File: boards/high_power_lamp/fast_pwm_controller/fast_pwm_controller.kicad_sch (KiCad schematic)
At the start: 22 parts, among them J1 Screw_Terminal_01x02, J2 Screw_Terminal_01x02, J3 Screw_Terminal_01x02, J4 Screw_Terminal_01x02, J5 Screw_Terminal_01x02, J6 Screw_Terminal_01x02, J7 Screw_Terminal_01x02, J8 Screw_Terminal_01x02, J9 Screw_Terminal_01x02, U2 TLC3704

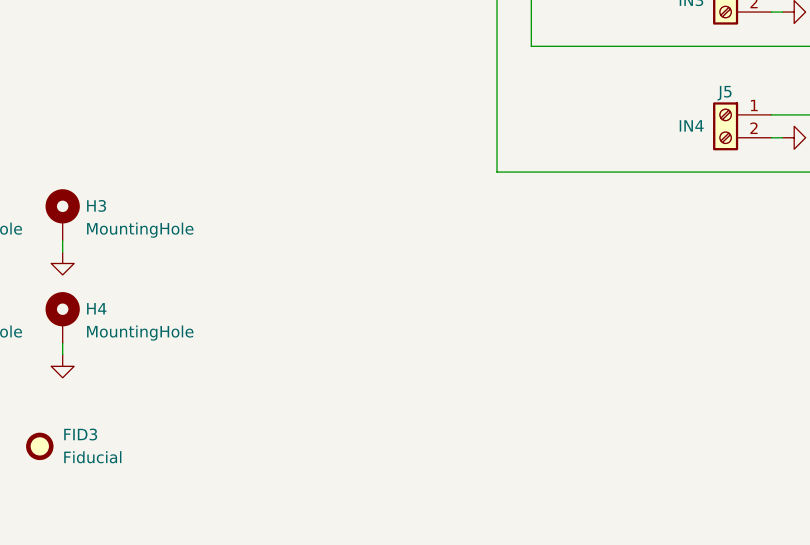
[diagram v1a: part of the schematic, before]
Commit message: basic external layout of board
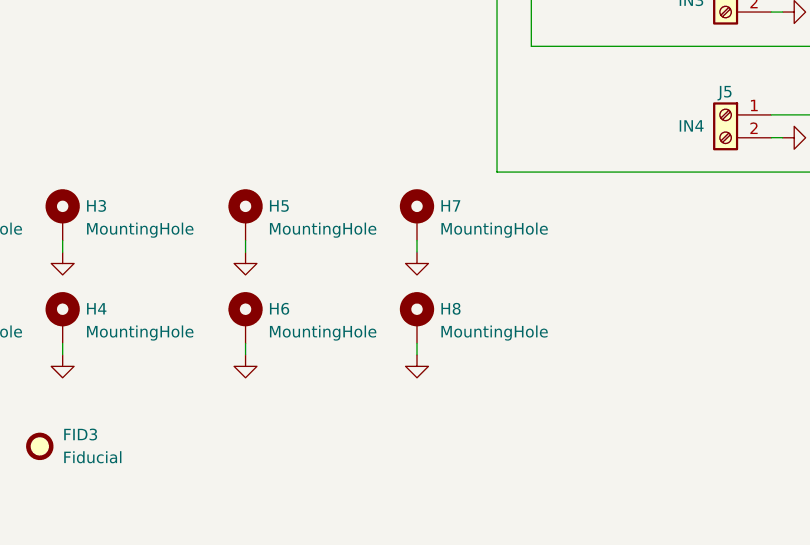
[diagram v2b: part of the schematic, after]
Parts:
- added H5, H6, H7, H8: MountingHole, MountingHole:MountingHole_3.2mm_M3_DIN965_Pad, symbol Mechanical:MountingHole_Pad
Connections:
- net GND: now also H5.1, H6.1, H7.1, H8.1

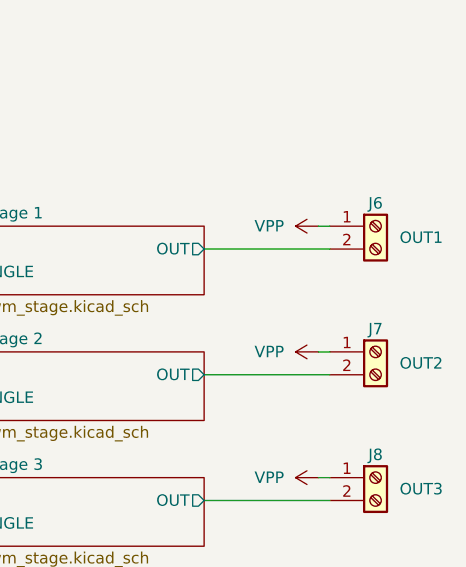
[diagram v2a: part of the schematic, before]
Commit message: almost finish arranging the fast pwm controller pcb
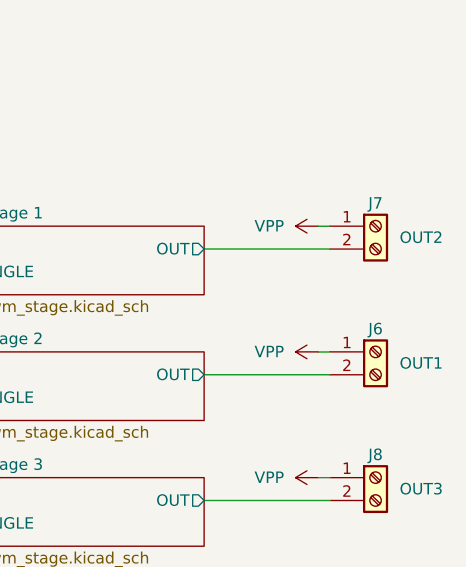
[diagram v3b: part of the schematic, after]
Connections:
- net PWM stage 1/OUT: now also J7.2 (Pin_2); no longer J6.2 (Pin_2)
- net PWM stage 2/OUT: now also J6.2 (Pin_2); no longer J7.2 (Pin_2)
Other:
- moved on the sheet: J6, J7
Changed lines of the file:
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@@
     )
   )
-  (symbol (lib_id "Connector:Screw_Terminal_01x02") (at 208.28 93.98 0) (unit 1)
+  (symbol (lib_id "Connector:Screw_Terminal_01x02") (at 208.28 107.95 0) (unit 1)
     (in_bom yes) (on_board yes) (dnp no)
-    (property "Reference" "J6" (at 208.28 91.44 0)
+    (property "Reference" "J6" (at 208.28 105.41 0)
       (effects (font (size 1.27 1.27)))
     )
-    (property "Value" "Screw_Terminal_01x02" (at 208.28 100.33 0)
+    (property "Value" "Screw_Terminal_01x02" (at 208.28 114.3 0)
       (effects (font (size 1.27 1.27)) hide)
     )
-    (property "Footprint" "TerminalBlock_Philmore:TerminalBlock_Philmore_TB132_1x02_P5.00mm_Horizontal" (at 208.28 93.98 0)
+    (property "Footprint" "TerminalBlock_Philmore:TerminalBlock_Philmore_TB132_1x02_P5.00mm_Horizontal" (at 208.28 107.95 0)
       (effects (font (size 1.27 1.27)) hide)
     )
-    (property "Datasheet" "~" (at 208.28 93.98 0)
+    (property "Datasheet" "~" (at 208.28 107.95 0)
       (effects (font (size 1.27 1.27)) hide)
     )
-    (property "Purpose" "OUT1" (at 213.36 95.25 0)
+    (property "Purpose" "OUT1" (at 213.36 109.22 0)
       (effects (font (size 1.27 1.27)))
     )
@@
     )
   )
-  (symbol (lib_id "Connector:Screw_Terminal_01x02") (at 208.28 107.95 0) (unit 1)
+  (symbol (lib_id "Connector:Screw_Terminal_01x02") (at 208.28 93.98 0) (unit 1)
     (in_bom yes) (on_board yes) (dnp no)
-    (property "Reference" "J7" (at 208.28 105.41 0)
+    (property "Reference" "J7" (at 208.28 91.44 0)
       (effects (font (size 1.27 1.27)))
     )
-    (property "Value" "Screw_Terminal_01x02" (at 208.28 114.3 0)
+    (property "Value" "Screw_Terminal_01x02" (at 208.28 100.33 0)
       (effects (font (size 1.27 1.27)) hide)
     )
-    (property "Footprint" "TerminalBlock_Philmore:TerminalBlock_Philmore_TB132_1x02_P5.00mm_Horizontal" (at 208.28 107.95 0)
+    (property "Footprint" "TerminalBlock_Philmore:TerminalBlock_Philmore_TB132_1x02_P5.00mm_Horizontal" (at 208.28 93.98 0)
       (effects (font (size 1.27 1.27)) hide)
     )
-    (property "Datasheet" "~" (at 208.28 107.95 0)
+    (property "Datasheet" "~" (at 208.28 93.98 0)
       (effects (font (size 1.27 1.27)) hide)
     )
-    (property "Purpose" "OUT2" (at 213.36 109.22 0)
+    (property "Purpose" "OUT2" (at 213.36 95.25 0)
       (effects (font (size 1.27 1.27)))
     )

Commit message: prepare traces
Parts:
- renumbered J7 to J6, J6 to J7
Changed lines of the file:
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@@
   (symbol (lib_id "Connector:Screw_Terminal_01x02") (at 208.28 107.95 0) (unit 1)
     (in_bom yes) (on_board yes) (dnp no)
-    (property "Reference" "J6" (at 208.28 105.41 0)
+    (property "Reference" "J7" (at 208.28 105.41 0)
       (effects (font (size 1.27 1.27)))
     )
@@
       (project "fast_pwm_controller"
         (path "/ebb02bb0-15d4-41b5-b7b0-053d51d38d86"
-          (reference "J6") (unit 1)
+          (reference "J7") (unit 1)
         )
       )
@@
   (symbol (lib_id "Connector:Screw_Terminal_01x02") (at 208.28 93.98 0) (unit 1)
     (in_bom yes) (on_board yes) (dnp no)
-    (property "Reference" "J7" (at 208.28 91.44 0)
+    (property "Reference" "J6" (at 208.28 91.44 0)
       (effects (font (size 1.27 1.27)))
     )
@@
       (project "fast_pwm_controller"
         (path "/ebb02bb0-15d4-41b5-b7b0-053d51d38d86"
-          (reference "J7") (unit 1)
+          (reference "J6") (unit 1)
         )
       )

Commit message: arrange everything
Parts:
- gave numbers to parts that had none: 1
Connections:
- net +12V: now also U1.1 (VCC)
- net GND: now also U1.11, U1.14, U1.8 (VSS); no longer U1.3, U1.3
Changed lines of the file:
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@@
       )
       (project "fast_pwm_controller"
-        (path "/ebb02bb0-15d4-41b5-b7b0-053d51d38d86/14949cb1-4b69-4c50-91f5-b66762a055b9"
-          (reference "C?") (unit 1)
-        )
         (path "/ebb02bb0-15d4-41b5-b7b0-053d51d38d86"
           (reference "C1") (unit 1)
@@
     )
   )
-  (symbol (lib_id "4xxx:4050") (at 143.51 54.61 0) (unit 1)
-    (in_bom yes) (on_board yes) (dnp no)
-    (property "Reference" "U?" (at 147.32 45.72 0)
+  (symbol (lib_id "4xxx:4050") (at 143.51 54.61 0) (unit 7)
+    (in_bom yes) (on_board yes) (dnp no)
+    (property "Reference" "U1" (at 147.32 45.72 0)
       (effects (font (size 1.27 1.27)))
     )
@@
     (instances
       (project "fast_pwm_controller"
-        (path "/ebb02bb0-15d4-41b5-b7b0-053d51d38d86/1dc02105-34f4-4dcd-909a-a43f3cf6326e"
-          (reference "U?") (unit 1)
-        )
         (path "/ebb02bb0-15d4-41b5-b7b0-053d51d38d86"
           (reference "U1") (unit 7)
@@
     )
   )
-  (symbol (lib_id "4xxx:4050") (at 207.01 50.8 0) (unit 1)
-    (in_bom yes) (on_board yes) (dnp no)
-    (property "Reference" "U?" (at 207.01 45.72 0)
+  (symbol (lib_id "4xxx:4050") (at 207.01 50.8 0) (unit 5)
+    (in_bom yes) (on_board yes) (dnp no)
+    (property "Reference" "U1" (at 207.01 45.72 0)
       (effects (font (size 1.27 1.27)))
     )
@@
     (instances
       (project "fast_pwm_controller"
-        (path "/ebb02bb0-15d4-41b5-b7b0-053d51d38d86/1dc02105-34f4-4dcd-909a-a43f3cf6326e"
-          (reference "U?") (unit 1)
-        )
         (path "/ebb02bb0-15d4-41b5-b7b0-053d51d38d86"
           (reference "U1") (unit 5)
@@
       )
       (project "fast_pwm_controller"
-        (path "/ebb02bb0-15d4-41b5-b7b0-053d51d38d86/14949cb1-4b69-4c50-91f5-b66762a055b9"
-          (reference "C?") (unit 1)
-        )
         (path "/ebb02bb0-15d4-41b5-b7b0-053d51d38d86"
           (reference "C2") (unit 1)
@@
     )
   )
-  (symbol (lib_id "4xxx:4050") (at 207.01 62.23 0) (unit 1)
-    (in_bom yes) (on_board yes) (dnp no)
-    (property "Reference" "U?" (at 207.01 57.15 0)
+  (symbol (lib_id "4xxx:4050") (at 207.01 62.23 0) (unit 6)
+    (in_bom yes) (on_board yes) (dnp no)
+    (property "Reference" "U1" (at 207.01 57.15 0)
       (effects (font (size 1.27 1.27)))
     )
@@
     (instances
       (project "fast_pwm_controller"
-        (path "/ebb02bb0-15d4-41b5-b7b0-053d51d38d86/1dc02105-34f4-4dcd-909a-a43f3cf6326e"
-          (reference "U?") (unit 1)
-        )
         (path "/ebb02bb0-15d4-41b5-b7b0-053d51d38d86"
           (reference "U1") (unit 6)
@@
           (reference "U2") (unit 5)
         )
-        (path "/ebb02bb0-15d4-41b5-b7b0-053d51d38d86/1dc02105-34f4-4dcd-909a-a43f3cf6326e"
-          (reference "U?") (unit 1)
-        )
       )
     )
@@
       (effects (font (size 1.27 1.27)) hide)
     )
-    (property "Value" "+12V" (at 41.91 95.25 0)
+    (property "Value" "+12V" (at 39.37 95.25 90)
       (effects (font (size 1.27 1.27)))
     )
@@
       (effects (font (size 1.27 1.27)) (justify left top))
     )
-    (pin "TRIANGLE_INV" output (at 90.17 97.79 0)
+    (pin "TRIANGLE_INV" output (at 90.17 95.25 0)
       (effects (font (size 1.27 1.27)) (justify right))
     )
-    (pin "TRIANGLE" output (at 90.17 95.25 0)
+    (pin "TRIANGLE" output (at 90.17 97.79 0)
       (effects (font (size 1.27 1.27)) (justify right))
     )

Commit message: finalise board
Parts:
- added TP1, TP2: TestPoint, TestPoint:TestPoint_THTPad_D2.0mm_Drill1.0mm, symbol Connector:TestPoint
- J6: renamed from J9; Purpose OUT4 -> OUT1
- J7: renamed from J8; Purpose OUT3 -> OUT2
- J8: renamed from J6; Purpose OUT2 -> OUT3
- J9: renamed from J7; Purpose OUT1 -> OUT4
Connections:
- net PWM stage 1/OUT: now also J6.2 (Pin_2); no longer J8.2 (Pin_2)
- net PWM stage 1/TRIANGLE: now also TP1.1
- net PWM stage 2/OUT: now also J7.2 (Pin_2); no longer J9.2 (Pin_2)
- net PWM stage 2/TRIANGLE: now also TP2.1
- net PWM stage 3/OUT: now also J8.2 (Pin_2); no longer J7.2 (Pin_2)
- net PWM stage 4/OUT: now also J9.2 (Pin_2); no longer J6.2 (Pin_2)
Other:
- moved on the sheet: J6, J7, J8, J9
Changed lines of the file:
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@@
 (kicad_sch (version 20230121) (generator eeschema)
   (paper "A4")
+  (junction (at 99.06 97.79) (diameter 0) (color 0 0 0 0)
+  )
   (junction (at 115.57 113.03) (diameter 0) (color 0 0 0 0)
   )
@@
   )
   (junction (at 119.38 99.06) (diameter 0) (color 0 0 0 0)
+  )
+  (junction (at 99.06 95.25) (diameter 0) (color 0 0 0 0)
   )
   (junction (at 143.51 38.1) (diameter 0) (color 0 0 0 0)
@@
     (stroke (width 0) (type default))
   )
-  (wire (pts (xy 90.17 97.79) (xy 115.57 97.79))
+  (wire (pts (xy 90.17 97.79) (xy 99.06 97.79))
     (stroke (width 0) (type default))
   )
@@
     (stroke (width 0) (type default))
   )
+  (wire (pts (xy 99.06 95.25) (xy 119.38 95.25))
+    (stroke (width 0) (type default))
+  )
   (wire (pts (xy 146.05 123.19) (xy 147.32 123.19))
     (stroke (width 0) (type default))
@@
     (stroke (width 0) (type default))
   )
-  (wire (pts (xy 90.17 95.25) (xy 119.38 95.25))
+  (wire (pts (xy 90.17 95.25) (xy 99.06 95.25))
     (stroke (width 0) (type default))
   )
@@
   )
   (wire (pts (xy 157.48 58.42) (xy 157.48 69.85))
+    (stroke (width 0) (type default))
+  )
+  (wire (pts (xy 99.06 97.79) (xy 115.57 97.79))
     (stroke (width 0) (type default))
   )
@@
     )
   )
-  (symbol (lib_id "Connector:Screw_Terminal_01x02") (at 208.28 121.92 0) (unit 1)
-    (in_bom yes) (on_board yes) (dnp no)
-    (property "Reference" "J8" (at 208.28 119.38 0)
-      (effects (font (size 1.27 1.27)))
-    )
-    (property "Value" "Screw_Terminal_01x02" (at 208.28 128.27 0)
-      (effects (font (size 1.27 1.27)) hide)
-    )
-    (property "Footprint" "TerminalBlock_Philmore:TerminalBlock_Philmore_TB132_1x02_P5.00mm_Horizontal" (at 208.28 121.92 0)
-      (effects (font (size 1.27 1.27)) hide)
-    )
-    (property "Datasheet" "~" (at 208.28 121.92 0)
-      (effects (font (size 1.27 1.27)) hide)
-    )
-    (property "Purpose" "OUT3" (at 213.36 123.19 0)
+  (symbol (lib_id "Connector:Screw_Terminal_01x02") (at 208.28 107.95 0) (unit 1)
+    (in_bom yes) (on_board yes) (dnp no)
+    (property "Reference" "J7" (at 208.28 105.41 0)
+      (effects (font (size 1.27 1.27)))
+    )
+    (property "Value" "Screw_Terminal_01x02" (at 208.28 114.3 0)
+      (effects (font (size 1.27 1.27)) hide)
+    )
+    (property "Footprint" "TerminalBlock_Philmore:TerminalBlock_Philmore_TB132_1x02_P5.00mm_Horizontal" (at 208.28 107.95 0)
+      (effects (font (size 1.27 1.27)) hide)
+    )
+    (property "Datasheet" "~" (at 208.28 107.95 0)
+      (effects (font (size 1.27 1.27)) hide)
+    )
+    (property "Purpose" "OUT2" (at 213.36 109.22 0)
       (effects (font (size 1.27 1.27)))
     )
@@
       (project "fast_pwm_controller"
         (path "/ebb02bb0-15d4-41b5-b7b0-053d51d38d86"
-          (reference "J8") (unit 1)
+          (reference "J7") (unit 1)
         )
       )
@@
     )
   )
-  (symbol (lib_id "Connector:Screw_Terminal_01x02") (at 208.28 135.89 0) (unit 1)
-    (in_bom yes) (on_board yes) (dnp no)
-    (property "Reference" "J9" (at 208.28 133.35 0)
-      (effects (font (size 1.27 1.27)))
-    )
-    (property "Value" "Screw_Terminal_01x02" (at 208.28 142.24 0)
-      (effects (font (size 1.27 1.27)) hide)
-    )
-    (property "Footprint" "TerminalBlock_Philmore:TerminalBlock_Philmore_TB132_1x02_P5.00mm_Horizontal" (at 208.28 135.89 0)
-      (effects (font (size 1.27 1.27)) hide)
-    )
-    (property "Datasheet" "~" (at 208.28 135.89 0)
-      (effects (font (size 1.27 1.27)) hide)
-    )
-    (property "Purpose" "OUT4" (at 213.36 137.16 0)
+  (symbol (lib_id "Connector:TestPoint") (at 99.06 97.79 180) (unit 1)
+    (in_bom yes) (on_board yes) (dnp no) (fields_autoplaced)
+    (property "Reference" "TP2" (at 101.6 101.092 0)
+      (effects (font (size 1.27 1.27)) (justify right))
+    )
+    (property "Value" "TestPoint" (at 101.6 102.362 0)
+      (effects (font (size 1.27 1.27)) (justify right) hide)
+    )
+    (property "Footprint" "TestPoint:TestPoint_THTPad_D2.0mm_Drill1.0mm" (at 93.98 97.79 0)
+      (effects (font (size 1.27 1.27)) hide)
+    )
+    (property "Datasheet" "~" (at 93.98 97.79 0)
+      (effects (font (size 1.27 1.27)) hide)
+    )
+    (pin "1")
+    (instances
+      (project "fast_pwm_controller"
+        (path "/ebb02bb0-15d4-41b5-b7b0-053d51d38d86"
+          (reference "TP2") (unit 1)
+        )
+      )
+    )
+  )
+  (symbol (lib_id "Connector:Screw_Terminal_01x02") (at 208.28 93.98 0) (unit 1)
+    (in_bom yes) (on_board yes) (dnp no)
+    (property "Reference" "J6" (at 208.28 91.44 0)
+      (effects (font (size 1.27 1.27)))
+    )
+    (property "Value" "Screw_Terminal_01x02" (at 208.28 100.33 0)
+      (effects (font (size 1.27 1.27)) hide)
+    )
+    (property "Footprint" "TerminalBlock_Philmore:TerminalBlock_Philmore_TB132_1x02_P5.00mm_Horizontal" (at 208.28 93.98 0)
+      (effects (font (size 1.27 1.27)) hide)
+    )
+    (property "Datasheet" "~" (at 208.28 93.98 0)
+      (effects (font (size 1.27 1.27)) hide)
+    )
+    (property "Purpose" "OUT1" (at 213.36 95.25 0)
       (effects (font (size 1.27 1.27)))
     )
@@
       (project "fast_pwm_controller"
         (path "/ebb02bb0-15d4-41b5-b7b0-053d51d38d86"
-          (reference "J9") (unit 1)
+          (reference "J6") (unit 1)
         )
       )
@@
     )
   )
-  (symbol (lib_id "Connector:Screw_Terminal_01x02") (at 208.28 107.95 0) (unit 1)
-    (in_bom yes) (on_board yes) (dnp no)
-    (property "Reference" "J7" (at 208.28 105.41 0)
-      (effects (font (size 1.27 1.27)))
-    )
-    (property "Value" "Screw_Terminal_01x02" (at 208.28 114.3 0)
-      (effects (font (size 1.27 1.27)) hide)
-    )
-    (property "Footprint" "TerminalBlock_Philmore:TerminalBlock_Philmore_TB132_1x02_P5.00mm_Horizontal" (at 208.28 107.95 0)
-      (effects (font (size 1.27 1.27)) hide)
-    )
-    (property "Datasheet" "~" (at 208.28 107.95 0)
-      (effects (font (size 1.27 1.27)) hide)
-    )
-    (property "Purpose" "OUT1" (at 213.36 109.22 0)
+  (symbol (lib_id "Connector:Screw_Terminal_01x02") (at 208.28 135.89 0) (unit 1)
+    (in_bom yes) (on_board yes) (dnp no)
+    (property "Reference" "J9" (at 208.28 133.35 0)
+      (effects (font (size 1.27 1.27)))
+    )
+    (property "Value" "Screw_Terminal_01x02" (at 208.28 142.24 0)
+      (effects (font (size 1.27 1.27)) hide)
+    )
+    (property "Footprint" "TerminalBlock_Philmore:TerminalBlock_Philmore_TB132_1x02_P5.00mm_Horizontal" (at 208.28 135.89 0)
+      (effects (font (size 1.27 1.27)) hide)
+    )
+    (property "Datasheet" "~" (at 208.28 135.89 0)
+      (effects (font (size 1.27 1.27)) hide)
+    )
+    (property "Purpose" "OUT4" (at 213.36 137.16 0)
       (effects (font (size 1.27 1.27)))
     )
@@
       (project "fast_pwm_controller"
         (path "/ebb02bb0-15d4-41b5-b7b0-053d51d38d86"
-          (reference "J7") (unit 1)
+          (reference "J9") (unit 1)
         )
       )
@@
     )
   )
-  (symbol (lib_id "Connector:Screw_Terminal_01x02") (at 208.28 93.98 0) (unit 1)
-    (in_bom yes) (on_board yes) (dnp no)
-    (property "Reference" "J6" (at 208.28 91.44 0)
-      (effects (font (size 1.27 1.27)))
-    )
-    (property "Value" "Screw_Terminal_01x02" (at 208.28 100.33 0)
-      (effects (font (size 1.27 1.27)) hide)
-    )
-    (property "Footprint" "TerminalBlock_Philmore:TerminalBlock_Philmore_TB132_1x02_P5.00mm_Horizontal" (at 208.28 93.98 0)
-      (effects (font (size 1.27 1.27)) hide)
-    )
-    (property "Datasheet" "~" (at 208.28 93.98 0)
-      (effects (font (size 1.27 1.27)) hide)
-    )
-    (property "Purpose" "OUT2" (at 213.36 95.25 0)
+  (symbol (lib_id "Connector:Screw_Terminal_01x02") (at 208.28 121.92 0) (unit 1)
+    (in_bom yes) (on_board yes) (dnp no)
+    (property "Reference" "J8" (at 208.28 119.38 0)
+      (effects (font (size 1.27 1.27)))
+    )
+    (property "Value" "Screw_Terminal_01x02" (at 208.28 128.27 0)
+      (effects (font (size 1.27 1.27)) hide)
+    )
+    (property "Footprint" "TerminalBlock_Philmore:TerminalBlock_Philmore_TB132_1x02_P5.00mm_Horizontal" (at 208.28 121.92 0)
+      (effects (font (size 1.27 1.27)) hide)
+    )
+    (property "Datasheet" "~" (at 208.28 121.92 0)
+      (effects (font (size 1.27 1.27)) hide)
+    )
+    (property "Purpose" "OUT3" (at 213.36 123.19 0)
       (effects (font (size 1.27 1.27)))
     )
@@
       (project "fast_pwm_controller"
         (path "/ebb02bb0-15d4-41b5-b7b0-053d51d38d86"
-          (reference "J6") (unit 1)
+          (reference "J8") (unit 1)
         )
       )
@@
         )
       )
+    )
+  )
+  (symbol (lib_id "Connector:TestPoint") (at 99.06 95.25 0) (unit 1)
+    (in_bom yes) (on_board yes) (dnp no) (fields_autoplaced)
+    (property "Reference" "TP1" (at 101.6 91.948 0)
+      (effects (font (size 1.27 1.27)) (justify left))
+    )
+    (property "Value" "TestPoint" (at 101.6 93.218 0)
+      (effects (font (size 1.27 1.27)) (justify left) hide)
+    )
+    (property "Footprint" "TestPoint:TestPoint_THTPad_D2.0mm_Drill1.0mm" (at 104.14 95.25 0)
+      (effects (font (size 1.27 1.27)) hide)
+    )
+    (property "Datasheet" "~" (at 104.14 95.25 0)
+      (effects (font (size 1.27 1.27)) hide)
+    )
+    (pin "1")
+    (instances
+      (project "fast_pwm_controller"
+        (path "/ebb02bb0-15d4-41b5-b7b0-053d51d38d86"
+          (reference "TP1") (unit 1)
+        )
+      )
